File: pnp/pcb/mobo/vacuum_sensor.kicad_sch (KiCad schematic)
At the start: 8 parts, among them U2 TL072, U3 XGZP101SB1, U6 2SMPP-03, U7 INA128

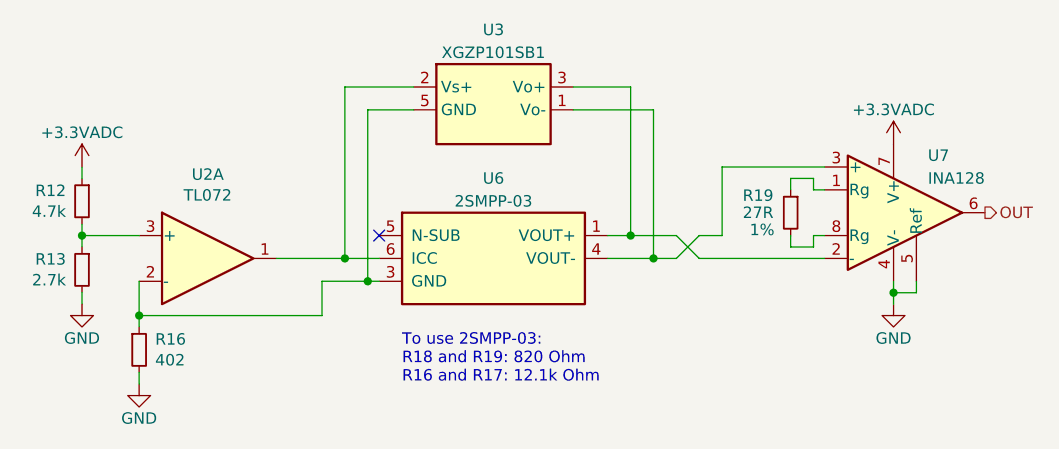
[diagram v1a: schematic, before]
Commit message: another huge chunk of work on rev04 of the mobo. breaks out diag and index pin for TMC2209 sensorless homing. reduces unique part count by consolidating resistor values where possible. replaces full ADC pipeline with monolithic I2C vacuum sensor and an I2C multiplexer due to address collision issues with two sensors. adds solder selectable jumpers for selecting whether an axis uses switch or TMC homing. redoes lots of routing of the SPI lines up to the stepper drivers.
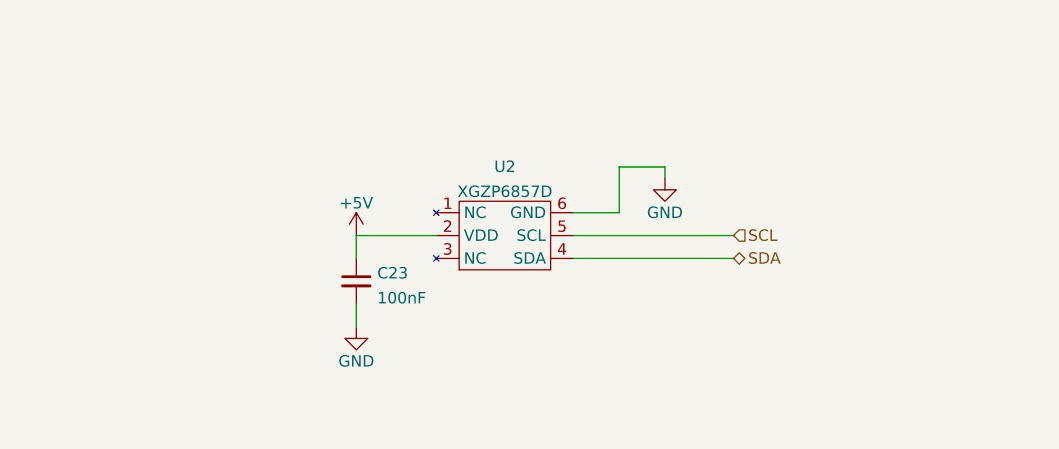
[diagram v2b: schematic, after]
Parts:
- removed R12: 4.7k, Resistor_SMD:R_0805_2012Metric, symbol Device:R_Small
- removed R13: 2.7k, Resistor_SMD:R_0805_2012Metric, symbol Device:R_Small
- removed R16: 402, Resistor_SMD:R_0805_2012Metric, symbol Device:R_Small
- removed R19: 27R, Resistor_SMD:R_0805_2012Metric, symbol Device:R_Small
- removed U2: TL072, Package_SO:SOIC-8_3.9x4.9mm_P1.27mm, symbol Amplifier_Operational:TL072
- removed U3: XGZP101SB1, index:SO-6_7x7mm_P2.54mm, symbol index:XGZP
- removed U6: 2SMPP-03, index:2SMPP-03, symbol index:2SMPP-03
- removed U7: INA128, Package_SO:SOIC-8_3.9x4.9mm_P1.27mm, symbol Amplifier_Instrumentation:INA128
- added C23: 100nF, Capacitor_SMD:C_0805_2012Metric, symbol Device:C_Small
- added U2: XGZP6857D, index:XGZP6857D, symbol index:XGZP6857D
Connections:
- net GND: now also C23.2, U2.6 (GND)
- new net +5V: C23.1, U2.2 (VDD)
- new net SCL: U2.5 (SCL)
- new net SDA: U2.4 (SDA)
- no-connect marks 1 -> 0
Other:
- note removed: "To use 2SMPP-03: R18 and R19: 820 Ohm R16 and R17: 12.1k Ohm"
